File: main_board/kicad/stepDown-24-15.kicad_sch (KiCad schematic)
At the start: 0 parts

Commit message: implemented 15v stepdown
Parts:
- added C1: C, symbol Device:C
- added C2: C_Polarized, symbol Device:C_Polarized
- added D1: 1N5822, Diode_THT:D_DO-201AD_P15.24mm_Horizontal, symbol Diode:1N5822
- added L1: L, symbol Device:L
- added U4: LM2576T-15, Package_TO_SOT_THT:TO-220-5_Vertical, symbol Regulator_Switching:LM2576T-15
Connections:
- new net: D1.1 (K), L1.1, U4.2 (OUT)
- new net +15V: C2.1, L1.2, U4.4 (FB)
- new net +24V: C1.1, U4.1 (VIN)
- new net GND: C1.2, C2.2, D1.2 (A), U4.3 (GND), U4.5 (~{ON}/OFF)

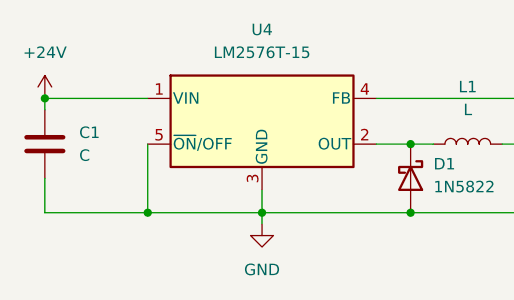
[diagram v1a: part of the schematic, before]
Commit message: added first capacitor value for stepdown
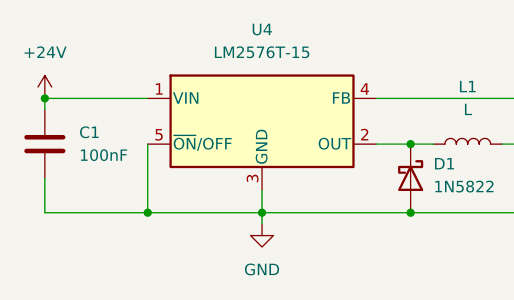
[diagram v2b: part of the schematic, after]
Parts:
- C1: value C -> 100nF
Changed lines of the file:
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@@
       (effects (font (size 1.27 1.27)) (justify left))
     )
-    (property "Value" "C" (at 125.73 104.1399 0)
+    (property "Value" "100nF" (at 125.73 104.1399 0)
       (effects (font (size 1.27 1.27)) (justify left))
     )

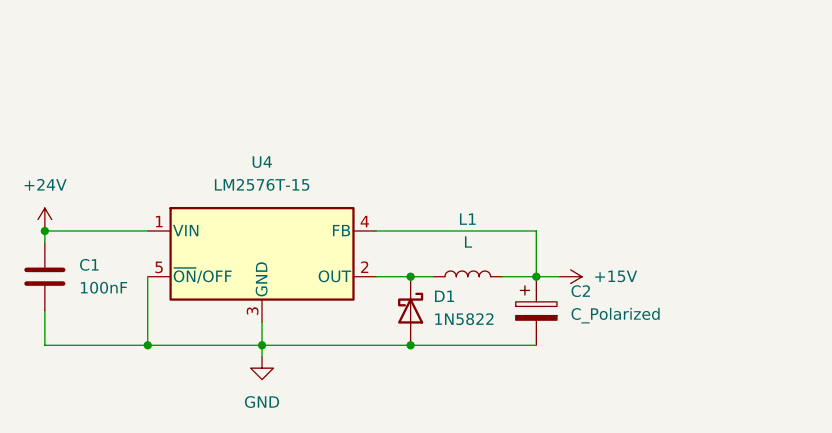
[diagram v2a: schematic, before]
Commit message: added LEDS and fuses
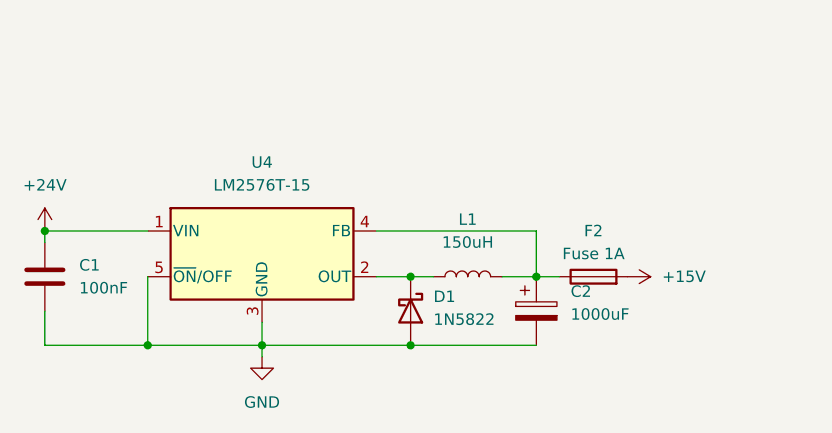
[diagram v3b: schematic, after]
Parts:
- added F2: Fuse 1A, symbol Device:Fuse
- C2: value C_Polarized -> 1000uF
- L1: value L -> 150uH
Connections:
- net +15V: now also F2.2; no longer C2.1, L1.2, U4.4 (FB)
- new net: C2.1, F2.1, L1.2, U4.4 (FB)
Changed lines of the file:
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@@
+    )
+  )
+  (symbol (lib_id "Device:Fuse") (at 182.88 102.87 90) (unit 1)
+    (in_bom yes) (on_board yes) (dnp no) (fields_autoplaced)
+    (property "Reference" "F2" (at 182.88 97.79 90)
+      (effects (font (size 1.27 1.27)))
+    )
+    (property "Value" "Fuse 1A" (at 182.88 100.33 90)
+      (effects (font (size 1.27 1.27)))
+    )
+    (property "Footprint" "" (at 182.88 104.648 90)
+      (effects (font (size 1.27 1.27)) hide)
+    )
+    (property "Datasheet" "~" (at 182.88 102.87 0)
+      (effects (font (size 1.27 1.27)) hide)
+    )
+    (pin "1")
+    (pin "2")
+    (instances
+      (project "main"
+        (path "/9139d8e7-a5dc-421f-9a12-f77d83384a16/4605f0e7-6d1c-410b-b12b-1c5d8b870a3a"
+          (reference "F2") (unit 1)
+        )
+      )
     )
   )
@@
     )
   )
-  (symbol (lib_id "power:+15V") (at 179.07 102.87 270) (unit 1)
+  (symbol (lib_id "power:+15V") (at 186.69 102.87 270) (unit 1)
     (in_bom yes) (on_board yes) (dnp no) (fields_autoplaced)
-    (property "Reference" "#PWR022" (at 175.26 102.87 0)
+    (property "Reference" "#PWR022" (at 182.88 102.87 0)
       (effects (font (size 1.27 1.27)) hide)
     )
-    (property "Value" "+15V" (at 182.88 102.87 90)
+    (property "Value" "+15V" (at 190.5 102.87 90)
       (effects (font (size 1.27 1.27)) (justify left))
     )
-    (property "Footprint" "" (at 179.07 102.87 0)
+    (property "Footprint" "" (at 186.69 102.87 0)
       (effects (font (size 1.27 1.27)) hide)
     )
-    (property "Datasheet" "" (at 179.07 102.87 0)
+    (property "Datasheet" "" (at 186.69 102.87 0)
       (effects (font (size 1.27 1.27)) hide)
     )
@@
       (effects (font (size 1.27 1.27)) (justify left))
     )
-    (property "Value" "C_Polarized" (at 180.34 107.061 0)
+    (property "Value" "1000uF" (at 180.34 107.061 0)
       (effects (font (size 1.27 1.27)) (justify left))
     )
@@
       (effects (font (size 1.27 1.27)))
     )
-    (property "Value" "L" (at 168.91 99.06 90)
+    (property "Value" "150uH" (at 168.91 99.06 90)
       (effects (font (size 1.27 1.27)))
     )

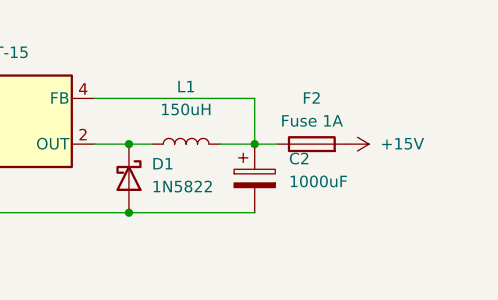
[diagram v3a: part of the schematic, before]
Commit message: resolved ERC
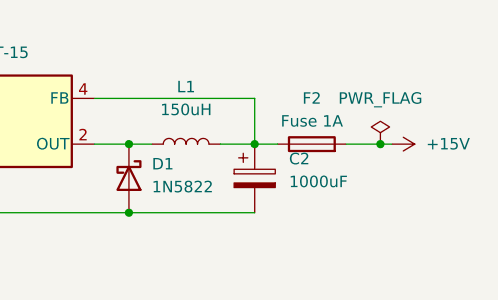
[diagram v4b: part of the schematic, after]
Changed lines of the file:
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@@
   (junction (at 133.35 110.49) (diameter 0) (color 0 0 0 0)
   )
+  (junction (at 190.5 102.87) (diameter 0) (color 0 0 0 0)
+  )
   (junction (at 176.53 102.87) (diameter 0) (color 0 0 0 0)
   )
   (junction (at 162.56 102.87) (diameter 0) (color 0 0 0 0)
   )
+  (wire (pts (xy 191.77 102.87) (xy 190.5 102.87))
+    (stroke (width 0) (type default))
+  )
   (wire (pts (xy 133.35 110.49) (xy 146.05 110.49))
     (stroke (width 0) (type default))
@@
     (stroke (width 0) (type default))
   )
+  (wire (pts (xy 190.5 102.87) (xy 186.69 102.87))
+    (stroke (width 0) (type default))
+  )
   (wire (pts (xy 162.56 102.87) (xy 165.1 102.87))
     (stroke (width 0) (type default))
@@
   (wire (pts (xy 172.72 102.87) (xy 176.53 102.87))
     (stroke (width 0) (type default))
+  )
+  (symbol (lib_id "power:PWR_FLAG") (at 190.5 102.87 0) (unit 1)
+    (in_bom yes) (on_board yes) (dnp no) (fields_autoplaced)
+    (property "Reference" "#FLG04" (at 190.5 100.965 0)
+      (effects (font (size 1.27 1.27)) hide)
+    )
+    (property "Value" "PWR_FLAG" (at 190.5 97.79 0)
+      (effects (font (size 1.27 1.27)))
+    )
+    (property "Footprint" "" (at 190.5 102.87 0)
+      (effects (font (size 1.27 1.27)) hide)
+    )
+    (property "Datasheet" "~" (at 190.5 102.87 0)
+      (effects (font (size 1.27 1.27)) hide)
+    )
+    (pin "1")
+    (instances
+      (project "main"
+        (path "/9139d8e7-a5dc-421f-9a12-f77d83384a16/4605f0e7-6d1c-410b-b12b-1c5d8b870a3a"
+          (reference "#FLG04") (unit 1)
+        )
+      )
+    )
   )
   (symbol (lib_id "Diode:1N5822") (at 162.56 106.68 270) (unit 1)
@@
     )
   )
-  (symbol (lib_id "power:+15V") (at 186.69 102.87 270) (unit 1)
-    (in_bom yes) (on_board yes) (dnp no) (fields_autoplaced)
-    (property "Reference" "#PWR022" (at 182.88 102.87 0)
-      (effects (font (size 1.27 1.27)) hide)
-    )
-    (property "Value" "+15V" (at 190.5 102.87 90)
-      (effects (font (size 1.27 1.27)) (justify left))
-    )
-    (property "Footprint" "" (at 186.69 102.87 0)
-      (effects (font (size 1.27 1.27)) hide)
-    )
-    (property "Datasheet" "" (at 186.69 102.87 0)
-      (effects (font (size 1.27 1.27)) hide)
-    )
+  (symbol (lib_id "power:+15V") (at 191.77 102.87 270) (unit 1)
+    (in_bom yes) (on_board yes) (dnp no) (fields_autoplaced)
+    (property "Reference" "#PWR022" (at 187.96 102.87 0)
+      (effects (font (size 1.27 1.27)) hide)
+    )
+    (property "Value" "+15V" (at 195.58 102.87 90)
+      (effects (font (size 1.27 1.27)) (justify left))
+    )
+    (property "Footprint" "" (at 191.77 102.87 0)
+      (effects (font (size 1.27 1.27)) hide)
+    )
+    (property "Datasheet" "" (at 191.77 102.87 0)
+      (effects (font (size 1.27 1.27)) hide)
+    )

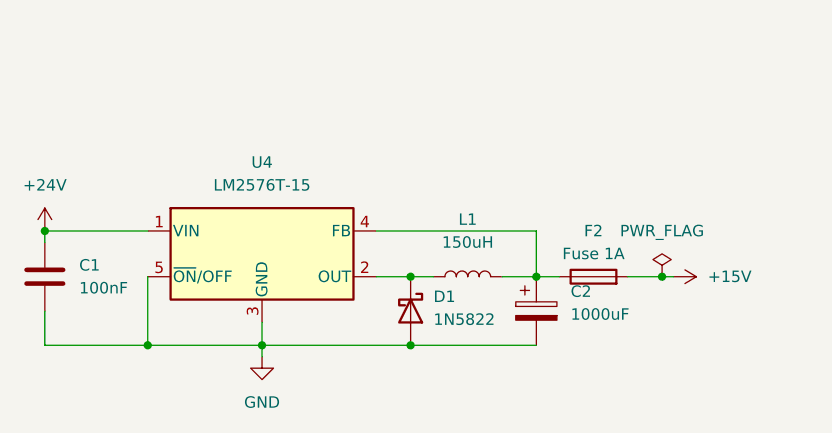
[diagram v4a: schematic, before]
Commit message: added probe point
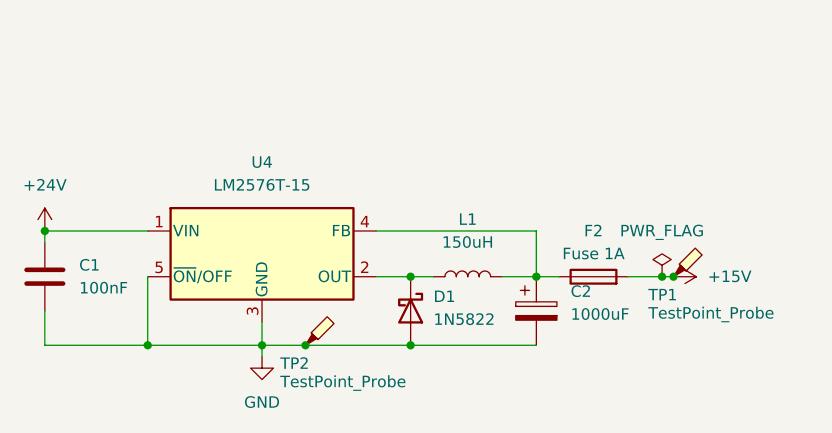
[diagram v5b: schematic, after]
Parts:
- added TP1, TP2: TestPoint_Probe, symbol Connector:TestPoint_Probe
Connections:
- net +15V: now also TP1.1
- net GND: now also TP2.1
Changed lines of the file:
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@@
 (kicad_sch (version 20230121) (generator eeschema)
   (paper "A4")
+  (junction (at 191.77 102.87) (diameter 0) (color 0 0 0 0)
+  )
   (junction (at 162.56 110.49) (diameter 0) (color 0 0 0 0)
   )
   (junction (at 121.92 97.79) (diameter 0) (color 0 0 0 0)
   )
+  (junction (at 150.876 110.49) (diameter 0) (color 0 0 0 0)
+  )
   (junction (at 146.05 110.49) (diameter 0) (color 0 0 0 0)
   )
@@
     (stroke (width 0) (type default))
   )
+  (wire (pts (xy 150.876 110.49) (xy 146.05 110.49))
+    (stroke (width 0) (type default))
+  )
   (wire (pts (xy 158.75 97.79) (xy 176.53 97.79))
     (stroke (width 0) (type default))
@@
     (stroke (width 0) (type default))
   )
-  (wire (pts (xy 162.56 110.49) (xy 146.05 110.49))
+  (wire (pts (xy 162.56 110.49) (xy 150.876 110.49))
     (stroke (width 0) (type default))
   )
@@
     )
   )
+  (symbol (lib_id "Connector:TestPoint_Probe") (at 150.876 110.49 0) (unit 1)
+    (in_bom yes) (on_board yes) (dnp no)
+    (property "Reference" "TP2" (at 148.082 112.522 0)
+      (effects (font (size 1.27 1.27)) (justify left))
+    )
+    (property "Value" "TestPoint_Probe" (at 148.082 114.554 0)
+      (effects (font (size 1.27 1.27)) (justify left))
+    )
+    (property "Footprint" "" (at 155.956 110.49 0)
+      (effects (font (size 1.27 1.27)) hide)
+    )
+    (property "Datasheet" "~" (at 155.956 110.49 0)
+      (effects (font (size 1.27 1.27)) hide)
+    )
+    (pin "1")
+    (instances
+      (project "main"
+        (path "/9139d8e7-a5dc-421f-9a12-f77d83384a16/4605f0e7-6d1c-410b-b12b-1c5d8b870a3a"
+          (reference "TP2") (unit 1)
+        )
+      )
+    )
+  )
   (symbol (lib_id "Device:C") (at 121.92 102.87 0) (unit 1)
     (in_bom yes) (on_board yes) (dnp no) (fields_autoplaced)
@@
         )
       )
+    )
+  )
+  (symbol (lib_id "Connector:TestPoint_Probe") (at 191.77 102.87 0) (unit 1)
+    (in_bom yes) (on_board yes) (dnp no)
+    (property "Reference" "TP1" (at 188.976 104.902 0)
+      (effects (font (size 1.27 1.27)) (justify left))
+    )
+    (property "Value" "TestPoint_Probe" (at 188.976 106.934 0)
+      (effects (font (size 1.27 1.27)) (justify left))
+    )
+    (property "Footprint" "" (at 196.85 102.87 0)
+      (effects (font (size 1.27 1.27)) hide)
+    )
+    (property "Datasheet" "~" (at 196.85 102.87 0)
+      (effects (font (size 1.27 1.27)) hide)
+    )
+    (pin "1")
+    (instances
+      (project "main"
+        (path "/9139d8e7-a5dc-421f-9a12-f77d83384a16/4605f0e7-6d1c-410b-b12b-1c5d8b870a3a"
+          (reference "TP1") (unit 1)
+        )
+      )

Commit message: updated to post review state
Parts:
- removed C1: 100nF, symbol Device:C
- removed TP1, TP2: TestPoint_Probe, symbol Connector:TestPoint_Probe
- added C23: 100uF, symbol Device:C_Polarized
- added TP3, TP4: TestPoint_Probe, symbol Connector:TestPoint_Probe
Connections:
- net +15V: now also C2.1, L1.2, U4.4 (FB), TP4.1; no longer F2.2
- net +24V: now also F2.2; no longer U4.1 (VIN)
- net GND: now also C23.2, TP3.1
- new net: C23.1, F2.1, U4.1 (VIN)
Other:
- moved on the sheet: F2

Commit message: corrected issues detected in review
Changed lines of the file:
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@@
   (junction (at 147.32 110.49) (diameter 0) (color 0 0 0 0)
   )
+  (junction (at 127.762 97.79) (diameter 0) (color 0 0 0 0)
+  )
   (junction (at 161.29 97.79) (diameter 0) (color 0 0 0 0)
   )
@@
     (stroke (width 0) (type default))
   )
-  (wire (pts (xy 121.92 97.79) (xy 133.35 97.79))
+  (wire (pts (xy 121.92 97.79) (xy 127.762 97.79))
+    (stroke (width 0) (type default))
+  )
+  (wire (pts (xy 121.92 80.518) (xy 121.92 82.55))
     (stroke (width 0) (type default))
   )
@@
   )
   (wire (pts (xy 158.75 97.79) (xy 161.29 97.79))
+    (stroke (width 0) (type default))
+  )
+  (wire (pts (xy 127.762 97.79) (xy 133.35 97.79))
     (stroke (width 0) (type default))
   )
@@
     )
   )
+  (symbol (lib_id "power:PWR_FLAG") (at 127.762 97.79 0) (unit 1)
+    (in_bom yes) (on_board yes) (dnp no) (fields_autoplaced)
+    (property "Reference" "#FLG05" (at 127.762 95.885 0)
+      (effects (font (size 1.27 1.27)) hide)
+    )
+    (property "Value" "PWR_FLAG" (at 127.762 92.71 0)
+      (effects (font (size 1.27 1.27)))
+    )
+    (property "Footprint" "" (at 127.762 97.79 0)
+      (effects (font (size 1.27 1.27)) hide)
+    )
+    (property "Datasheet" "~" (at 127.762 97.79 0)
+      (effects (font (size 1.27 1.27)) hide)
+    )
+    (pin "1")
+    (instances
+      (project "main"
+        (path "/9139d8e7-a5dc-421f-9a12-f77d83384a16/4605f0e7-6d1c-410b-b12b-1c5d8b870a3a"
+          (reference "#FLG05") (unit 1)
+        )
+      )
+    )
+  )
   (symbol (lib_id "Device:Fuse") (at 121.92 86.36 180) (unit 1)
     (in_bom yes) (on_board yes) (dnp no) (fields_autoplaced)
@@
     )
   )
-  (symbol (lib_id "power:+24V") (at 121.92 82.55 0) (unit 1)
-    (in_bom yes) (on_board yes) (dnp no) (fields_autoplaced)
-    (property "Reference" "#PWR08" (at 121.92 86.36 0)
-      (effects (font (size 1.27 1.27)) hide)
-    )
-    (property "Value" "+24V" (at 121.92 77.47 0)
-      (effects (font (size 1.27 1.27)))
-    )
-    (property "Footprint" "" (at 121.92 82.55 0)
-      (effects (font (size 1.27 1.27)) hide)
-    )
-    (property "Datasheet" "" (at 121.92 82.55 0)
-      (effects (font (size 1.27 1.27)) hide)
-    )
+  (symbol (lib_id "power:+24V") (at 121.92 80.518 0) (unit 1)
+    (in_bom yes) (on_board yes) (dnp no) (fields_autoplaced)
+    (property "Reference" "#PWR08" (at 121.92 84.328 0)
+      (effects (font (size 1.27 1.27)) hide)
+    )
+    (property "Value" "+24V" (at 121.92 75.438 0)
+      (effects (font (size 1.27 1.27)))
+    )
+    (property "Footprint" "" (at 121.92 80.518 0)
+      (effects (font (size 1.27 1.27)) hide)
+    )
+    (property "Datasheet" "" (at 121.92 80.518 0)
+      (effects (font (size 1.27 1.27)) hide)
+    )

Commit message: added footprints
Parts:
- C2: footprint (none) -> Capacitor_THT:CP_Radial_D10.0mm_P5.00mm
- C23: footprint (none) -> Capacitor_THT:CP_Radial_D6.3mm_P2.50mm
- F2: footprint (none) -> Fuse:Fuseholder_Cylinder-5x20mm_Schurter_0031_8201_Horizontal_Open
- L1: footprint (none) -> Inductor_THT:L_Radial_D12.5mm_P7.00mm_Fastron_09HCP
- TP3, TP4: footprint (none) -> TestPoint:TestPoint_Pad_D3.0mm
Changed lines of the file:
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@@
       (effects (font (size 1.27 1.27)) (justify left))
     )
-    (property "Footprint" "" (at 122.8852 106.68 0)
+    (property "Footprint" "Capacitor_THT:CP_Radial_D6.3mm_P2.50mm" (at 122.8852 106.68 0)
       (effects (font (size 1.27 1.27)) hide)
     )
@@
       (effects (font (size 1.27 1.27)) (justify right))
     )
-    (property "Footprint" "" (at 123.698 86.36 90)
+    (property "Footprint" "Fuse:Fuseholder_Cylinder-5x20mm_Schurter_0031_8201_Horizontal_Open" (at 123.698 86.36 90)
       (effects (font (size 1.27 1.27)) hide)
     )
@@
       (effects (font (size 1.27 1.27)) (justify left))
     )
-    (property "Footprint" "" (at 152.4 110.49 0)
+    (property "Footprint" "TestPoint:TestPoint_Pad_D3.0mm" (at 152.4 110.49 0)
       (effects (font (size 1.27 1.27)) hide)
     )
@@
       (effects (font (size 1.27 1.27)) (justify left))
     )
-    (property "Footprint" "" (at 166.37 97.79 0)
+    (property "Footprint" "TestPoint:TestPoint_Pad_D3.0mm" (at 166.37 97.79 0)
       (effects (font (size 1.27 1.27)) hide)
     )
@@
       (effects (font (size 1.27 1.27)) (justify left))
     )
-    (property "Footprint" "" (at 177.4952 110.49 0)
+    (property "Footprint" "Capacitor_THT:CP_Radial_D10.0mm_P5.00mm" (at 177.4952 110.49 0)
       (effects (font (size 1.27 1.27)) hide)
     )
@@
       (effects (font (size 1.27 1.27)))
     )
-    (property "Footprint" "" (at 168.91 102.87 0)
-      (effects (font (size 1.27 1.27)) hide)
-    )
+    (property "Footprint" "Inductor_THT:L_Radial_D12.5mm_P7.00mm_Fastron_09HCP" (at 168.91 102.87 0)
+      (effects (font (size 1.27 1.27)) hide)
+    )
